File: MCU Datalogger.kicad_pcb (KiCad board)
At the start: 2 copper layers, 0 parts

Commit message: Initail Layout
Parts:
- added BT1: Battery, Connector_PinHeader_2.54mm:PinHeader_1x02_P2.54mm_Vertical, F.Cu at (93.2, 65.0)
- added C1: .1uF, Capacitor_SMD:C_0805_2012Metric, F.Cu at (108.2, 64.7)
- added C2: 0.1uF, Capacitor_SMD:C_0805_2012Metric, F.Cu at (122.4, 71.3)
- added C3: 100nF, Capacitor_SMD:C_0805_2012Metric, F.Cu at (123.1, 76.2)
- added C4: 22pF, Capacitor_SMD:C_0805_2012Metric, F.Cu at (108.8, 73.4)
- added C5: 22pF, Capacitor_SMD:C_0805_2012Metric, F.Cu at (108.8, 75.5)
- added D1: LED, LED_SMD:LED_0805_2012Metric, F.Cu at (125.1, 67.9)
- added D2: LED, LED_SMD:LED_0805_2012Metric, F.Cu at (123.1, 74.1)
- added H1: MountingHole, MountingHole:MountingHole_2.1mm, F.Cu at (90.0, 60.0)
- added H2: MountingHole, MountingHole:MountingHole_2.1mm, F.Cu at (135.0, 59.8)
- added H3: MountingHole, MountingHole:MountingHole_2.1mm, F.Cu at (90.0, 84.5)
- added H4: MountingHole, MountingHole:MountingHole_2.1mm, F.Cu at (134.8, 84.8)
- added J1: Conn_01x04_Pin, Connector_PinHeader_2.54mm:PinHeader_1x04_P2.54mm_Vertical, F.Cu at (135.4, 72.8)
- added J2: Conn_01x04_Pin, Connector_PinHeader_2.54mm:PinHeader_1x04_P2.54mm_Vertical, F.Cu at (121.0, 85.0)
- added J3: Conn_01x09_Pin, Connector_PinHeader_2.54mm:PinHeader_1x09_P2.54mm_Vertical, F.Cu at (95.6, 85.0)
- added J4: Conn_02x03_Odd_Even, Connector_PinHeader_2.54mm:PinHeader_2x03_P2.54mm_Vertical, F.Cu at (132.9, 64.1)
- added R1: 10K, Resistor_SMD:R_0805_2012Metric, F.Cu at (113.0, 64.7)
- added R2: 10K, Resistor_SMD:R_0805_2012Metric, F.Cu at (110.6, 64.7)
- added R3: 330, Resistor_SMD:R_0805_2012Metric, F.Cu at (125.2, 70.7)
- added R4: 330, Resistor_SMD:R_0805_2012Metric, F.Cu at (126.8, 75.3)
- added R5: 10K, Resistor_SMD:R_0805_2012Metric, F.Cu at (115.4, 64.7)
- added R6: 4.7K, Resistor_SMD:R_0805_2012Metric, F.Cu at (117.8, 64.7)
- added R7: 4.7K, Resistor_SMD:R_0805_2012Metric, F.Cu at (120.2, 64.7)
- added U1: DS1337S_, DS1337S_:SOIC127P600X175-8N, F.Cu at (101.6, 78.3)
- added U2: ATMEGA328P-AU, ATMEGA328P-AU:QFP80P900X900X120-32N, F.Cu at (116.0, 71.9)
- added U3: 24LC1025, Package_SO:SOIC-8_5.23x5.23mm_P1.27mm, F.Cu at (101.7, 64.5)
- added U4: 24LC1025, Package_SO:SOIC-8_5.23x5.23mm_P1.27mm, F.Cu at (101.7, 71.9)
- added Y1: 32.768 KHz, Crystal:Crystal_SMD_5032-2Pin_5.0x3.2mm_HandSoldering, F.Cu at (94.1, 76.6)
- added Y2: 16MHz, Crystal:Crystal_SMD_5032-2Pin_5.0x3.2mm_HandSoldering, F.Cu at (113.2, 79.9)
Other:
- board outline added: 50 x 30 mm

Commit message: Initial Routing
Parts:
- moved J1 3.47 mm to (131.9, 72.5)
- moved J4 3.47 mm to (129.4, 63.8)
- moved J2 2.52 mm to (120.4, 82.5)
- moved J3 2.49 mm to (95.2, 82.5)
- moved C1 2.23 mm to (108.4, 62.5)
- moved R1 2.23 mm to (113.2, 62.5)
- moved R2 2.23 mm to (110.9, 62.5)
- moved R5 2.23 mm to (115.6, 62.5)
- moved R6 2.23 mm to (118.0, 62.5)
- moved R7 2.23 mm to (120.4, 62.5)
- moved Y2 1.42 mm to (113.2, 78.5)
- moved C4 1.41 mm to (108.7, 72.0)
- moved C5 1.41 mm to (108.7, 74.1)
- moved C3 1.40 mm to (123.1, 74.8)
- moved D1 1.40 mm to (125.1, 66.5)
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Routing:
- net /SCK: track 0.00 -> 85.0 mm, vias 0 -> 4
- net /VCC: track 0.00 -> 67.0 mm
- net /SDA: track 0.00 -> 54.6 mm, vias 0 -> 3
- net Net-(BT1-+): track 0.00 -> 38.1 mm
- net Net-(U1-~{INTA}): track 0.00 -> 27.3 mm, vias 0 -> 2
- net Net-(U2-PB6): track 0.00 -> 13.2 mm, vias 0 -> 2
- net Net-(U2-PB7): track 0.00 -> 7.06 mm
- net Net-(U1-X1): track 0.00 -> 6.04 mm
- net Net-(U1-X2): track 0.00 -> 5.64 mm
- net Net-(D2-K): track 0.00 -> 2.87 mm
- net Net-(D1-K): track 0.00 -> 2.76 mm
- net Net-(U2-AREF): track 0.00 -> 2.22 mm
- net /RESET: track 0.00 -> 2.21 mm
- net Net-(U1-SQW/~INT): track 0.00 -> 1.97 mm, vias 0 -> 1
- net GND: track 0.00 -> 1.37 mm, vias 0 -> 1
- added copper zone on B.Cu, net GND
- added copper zone on F.Cu, net GND
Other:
- outline, holes or cut-outs redrawn

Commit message: Layout complete
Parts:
- moved D1 0.21 mm to (125.3, 66.6)
- moved R3 0.21 mm to (125.3, 69.3)
- moved J2 0.15 mm to (120.4, 82.4)
- moved J3 0.15 mm to (95.2, 82.4)
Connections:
- BT1 pad 1: Net-(BT1-+) -> /VCC
- C3 pad 1: Net-(BT1-+) -> /VCC
- D2 pad 2: Net-(BT1-+) -> /VCC
- U2 pad 18: Net-(BT1-+) -> /VCC
- U2 pad 4: Net-(BT1-+) -> /VCC
- U2 pad 6: Net-(BT1-+) -> /VCC
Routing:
- net /VCC: track 67.0 -> 167.5 mm
- net Net-(BT1-+): track 38.1 -> 0.00 mm
- net GND: track 1.37 -> 35.0 mm, vias 1 -> 15
- net /D2: track 0.00 -> 31.2 mm, vias 0 -> 1
- net /MOSI: track 0.00 -> 25.8 mm, vias 0 -> 3
- net /D3: track 0.00 -> 25.1 mm, vias 0 -> 1
- net /TX: track 0.00 -> 25.0 mm, vias 0 -> 1
- net Net-(U1-SQW/~INT): track 1.97 -> 26.6 mm, vias 1 -> 2
- net /D4: track 0.00 -> 22.8 mm, vias 0 -> 1
- net /MISO: track 0.00 -> 21.0 mm, vias 0 -> 2
- net /RX: track 0.00 -> 20.6 mm, vias 0 -> 2
- net /RESET: track 2.21 -> 18.8 mm, vias 0 -> 1
- net /D6: track 0.00 -> 14.5 mm, vias 0 -> 1
- net /D5: track 0.00 -> 14.5 mm, vias 0 -> 1
- net /SCK: track 85.0 -> 99.3 mm
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- added copper zone on F.Cu, net /VCC
- removed copper zone on F.Cu, net GND

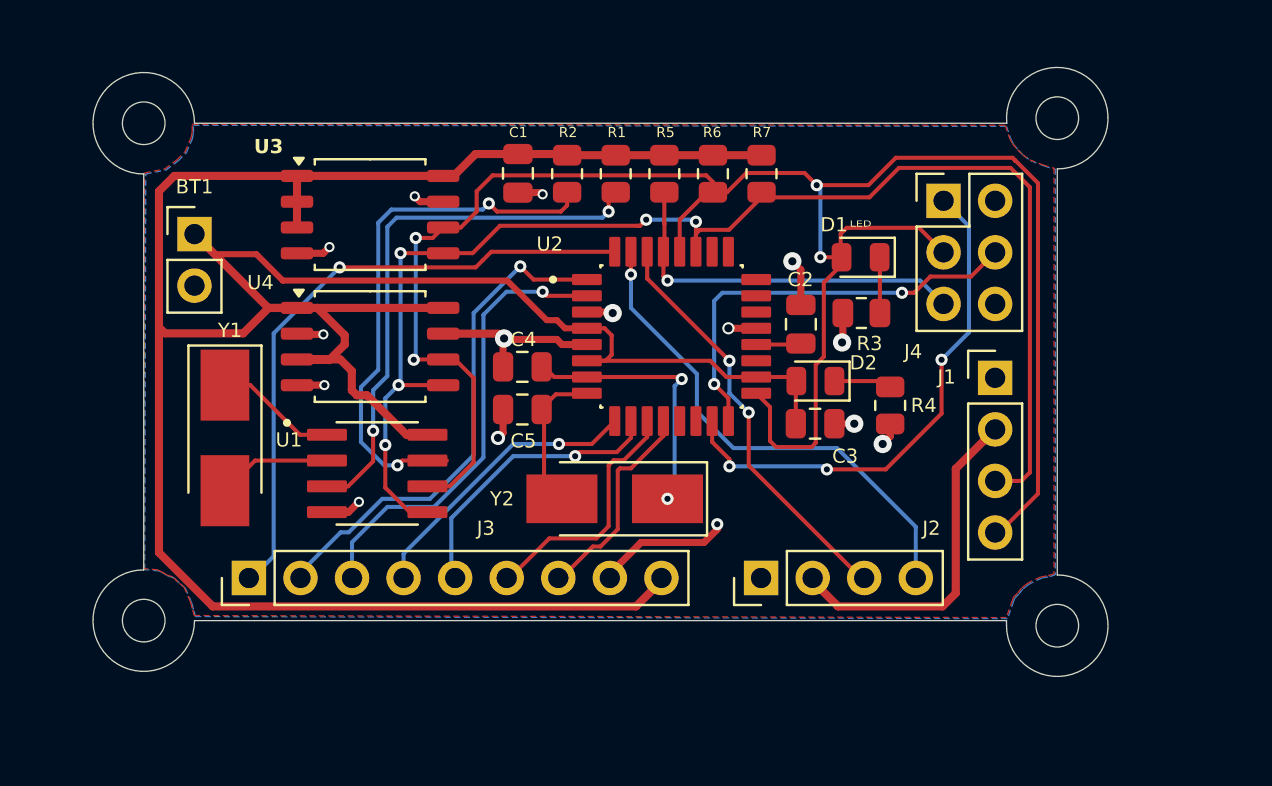
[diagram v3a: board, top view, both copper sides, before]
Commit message: SKILLSCREEN UPDATE
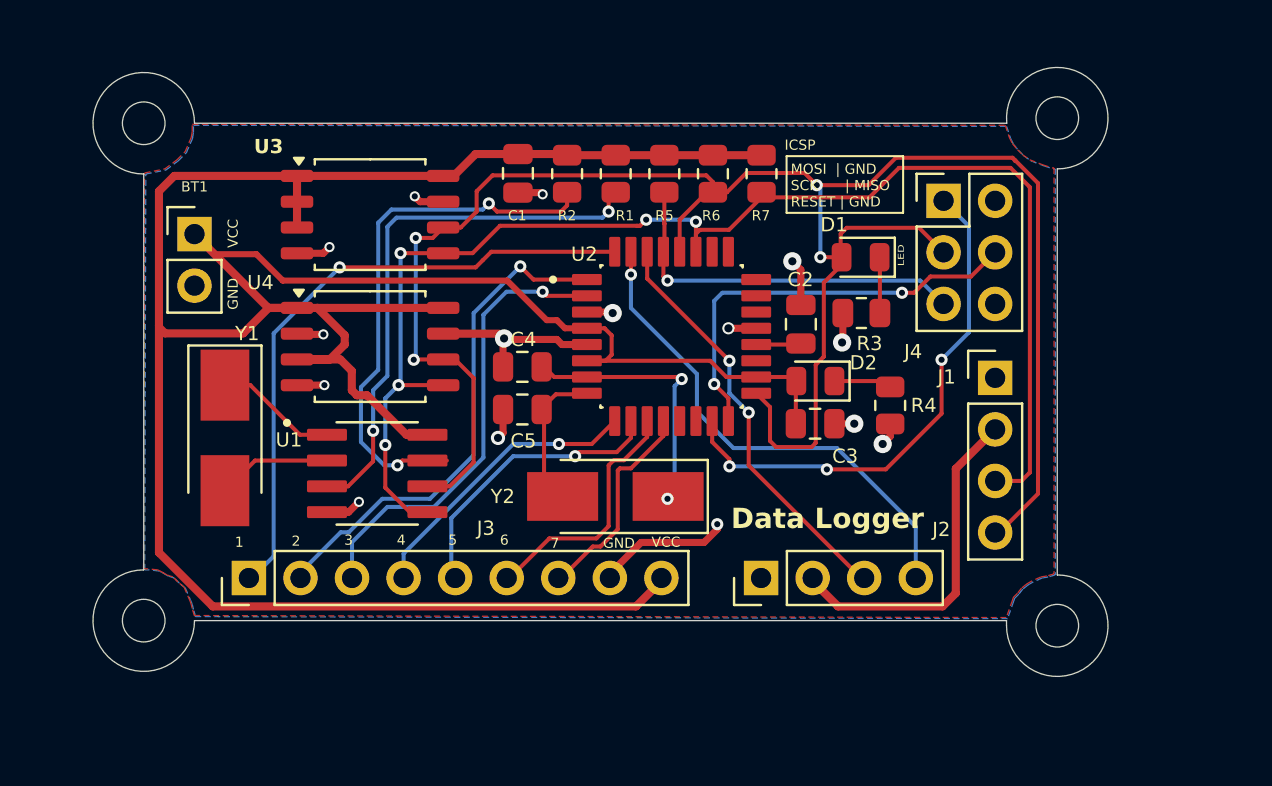
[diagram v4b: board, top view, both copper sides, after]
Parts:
- added REF**: WEEE-Logo_4.2x6mm_SilkScreen, Symbol:WEEE-Logo_4.2x6mm_SilkScreen, B.Cu at (93.5, 75.1)
- added REF**: KiCad-Logo2_5mm_SilkScreen, Symbol:KiCad-Logo2_5mm_SilkScreen, B.Cu at (112.9, 70.7)
- moved Y2 0.12 mm to (113.2, 78.4)
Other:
- board text added: "1"
- board text added: "2"
- board text added: "3"
- board text added: "4"
- board text added: "5"
- board text added: "6"
- board text added: "7"
- board text added: "Data Logger"
- board text added: "GND"
- board text added: "ICSP"
- board text added: "MOSI | GND SCK | MISO RESET | GND"
- board text added: "Md Nahidul Islam"
- board text added: "VCC"
